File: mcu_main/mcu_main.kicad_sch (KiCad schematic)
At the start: 9 parts, among them SW1 SW_Push_Dual, SW2 SW_Push_Dual, U1 ESP32-S3-WROOM-1

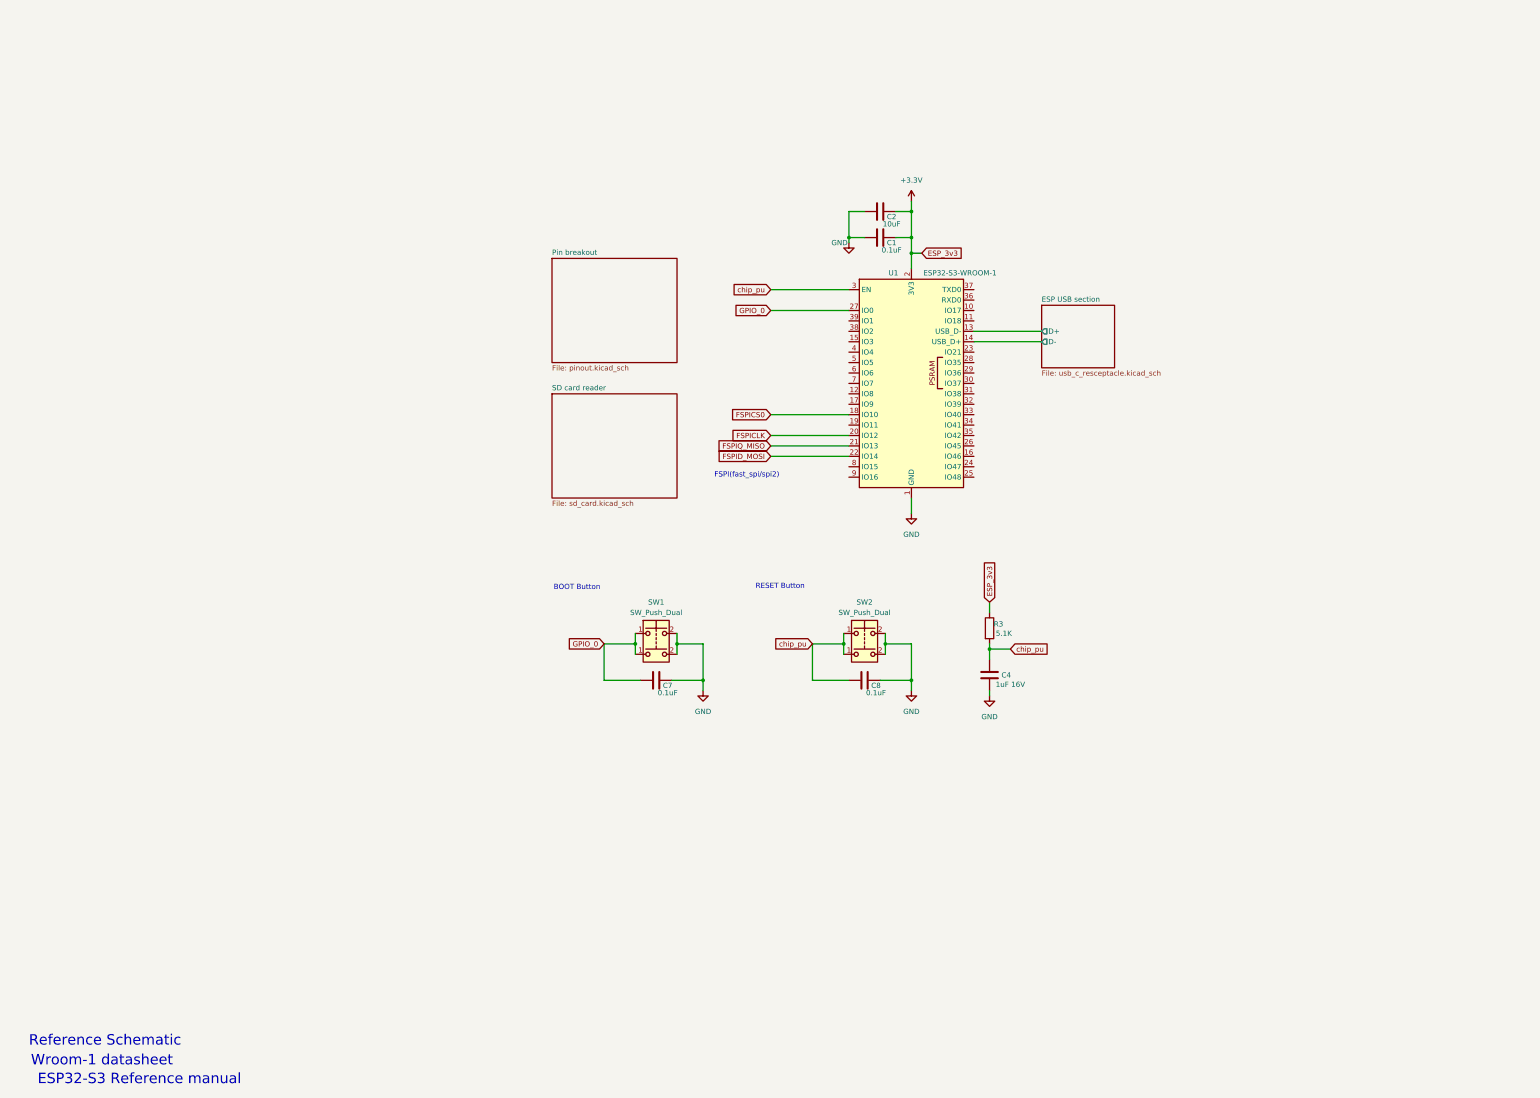
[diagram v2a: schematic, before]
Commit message: added I2C lines
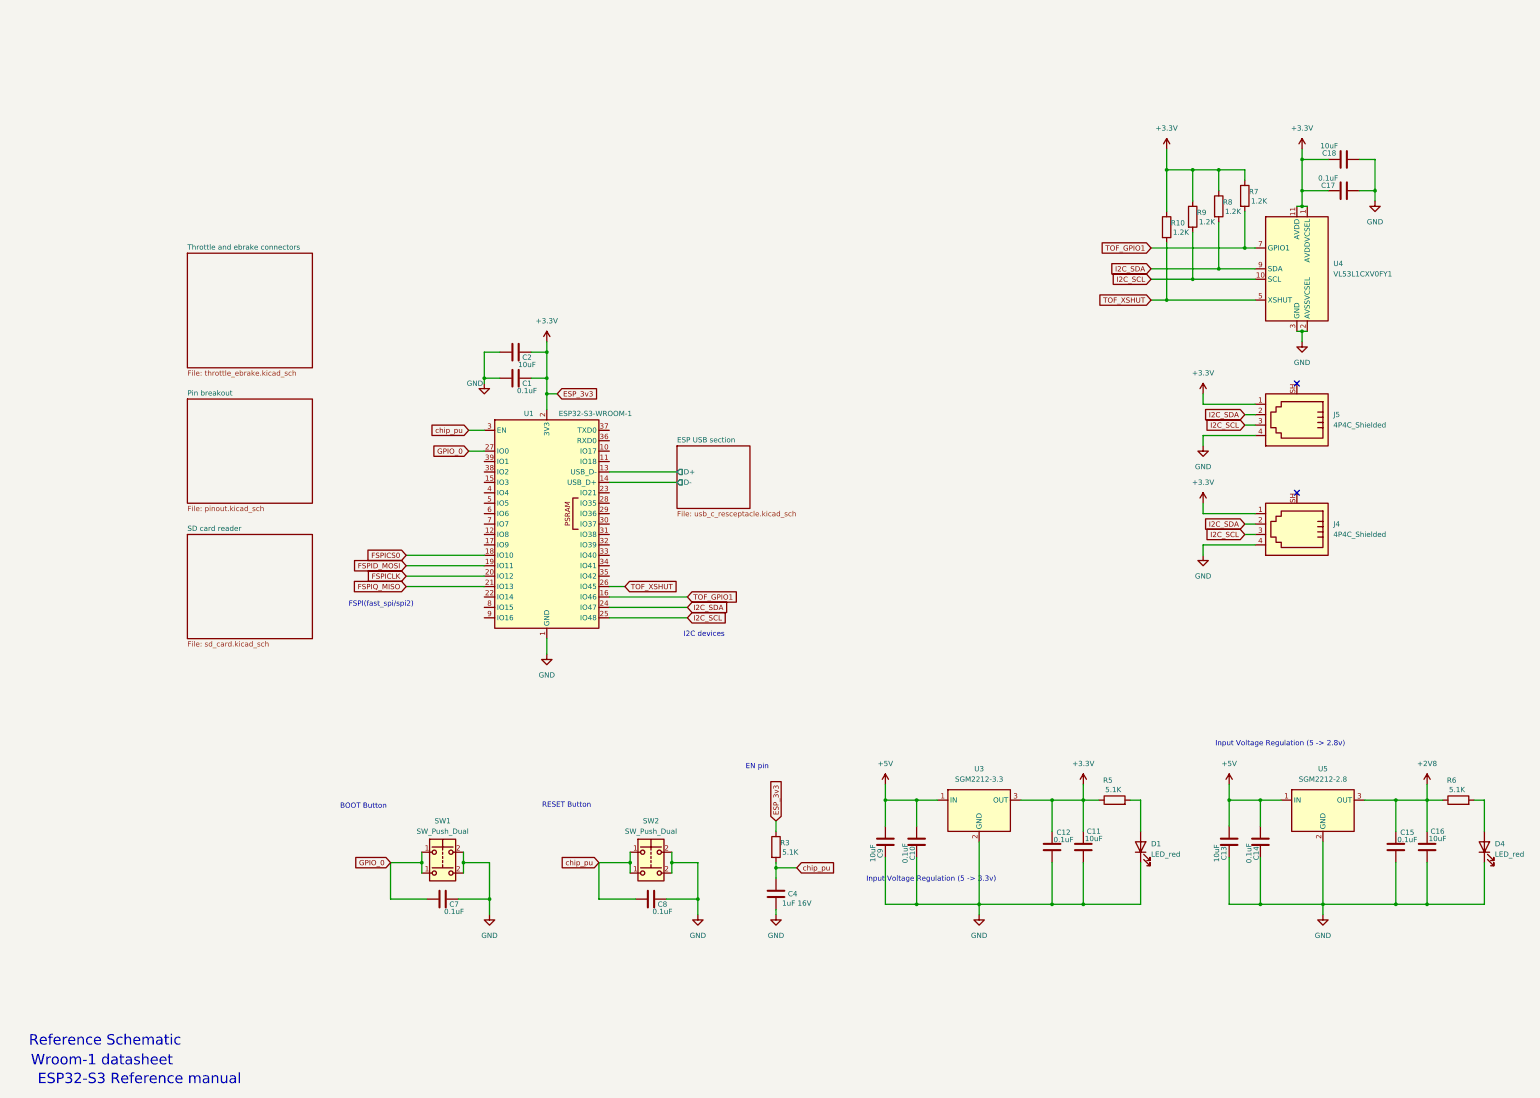
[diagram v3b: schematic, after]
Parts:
- added C10, C12, C14, C15, C17: 0.1uF, Capacitor_SMD:C_0603_1608Metric_Pad1.08x0.95mm_HandSolder, symbol Device:C
- added C11, C13, C16, C18, C9: 10uF, Capacitor_SMD:C_0603_1608Metric_Pad1.08x0.95mm_HandSolder, symbol Device:C
- added D1, D4: LED_red, LED_SMD:LED_0603_1608Metric_Pad1.05x0.95mm_HandSolder, symbol Device:LED
- added J4, J5: 4P4C_Shielded, Custom_footprints:JST_PH_4P_2mm_SMD, symbol Connector:4P4C_Shielded
- added R10, R7, R8, R9: 1.2K, Resistor_SMD:R_0805_2012Metric_Pad1.20x1.40mm_HandSolder, symbol Device:R
- added R5, R6: 5.1K, Resistor_SMD:R_0805_2012Metric_Pad1.20x1.40mm_HandSolder, symbol Device:R
- added U3: SGM2212-3.3, Package_TO_SOT_SMD:SOT-223-3_TabPin2, symbol Regulator_Linear:LT1963AxST-1.5
- added U4: VL53L1CXV0FY1, Sensor_Distance:ST_VL53L1x, symbol Sensor_Distance:VL53L1CXV0FY1
- added U5: SGM2212-2.8, Package_TO_SOT_SMD:SOT-223-3_TabPin2, symbol Regulator_Linear:LT1963AxST-1.5
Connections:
- net +3.3V: now also C11.2, C12.2, C17.2, C18.2, J4.1, J5.1, R10.1, R5.1, R7.1, R8.1, R9.1, U3.3 (OUT), U4.1 (AVDDVCSEL), U4.11 (AVDD)
- net FSPID_MOSI: now also U1.19 (IO11); no longer U1.22 (IO14)
- net GND: now also C10.2, C11.1, C12.1, C13.2, C14.2, C15.1, C16.1, C17.1, C18.1, C9.2, D1.1 (K), D4.1 (K), J4.4, J5.4, U3.2 (GND), U4.12 (GND), U4.2 (AVSSVCSEL), U4.3 (GND), U4.4 (GND), U4.6 (GND), U5.2 (GND)
- net TOF_GPIO1: now reaches U1.16 (IO46)
- net TOF_GPIO1: now also R7.2, U4.7 (GPIO1)
- net I2C_SDA: now reaches U1.24 (IO47)
- net I2C_SDA: now also J4.2, J5.2, R8.2, U4.9 (SDA)
- net I2C_SCL: now reaches U1.25 (IO48)
- net I2C_SCL: now also J4.3, J5.3, R9.2, U4.10 (SCL)
- net TOF_XSHUT: now reaches U1.26 (IO45)
- net TOF_XSHUT: now also R10.2, U4.5 (XSHUT)
- new net: D1.2 (A), R5.2
- new net: D4.2 (A), R6.2
- new net +2V8: C15.2, C16.2, R6.1, U5.3 (OUT)
- new net +5V: C10.1, C13.1, C14.1, C9.1, U3.1 (IN), U5.1 (IN)
- no-connect marks 0 -> 2
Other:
- added sheet Throttle and ebrake connectors (throttle_ebrake.kicad_sch)
- note added: "EN pin"
- note added: "I2C devices"
- note added: "Input Voltage Regulation (5 -> 2.8v)"
- note added: "Input Voltage Regulation (5 -> 3.3v)"
- moved on the sheet: C1, C2, C4, C7, C8, R3, SW1, SW2, U1
